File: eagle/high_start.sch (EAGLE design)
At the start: 34 parts, among them IC1 7805L, Q1 16Mhz, Q2 IRF510, Q3 IRF510, Q4 IRF510, U2 ATMEGA328P_PDIP

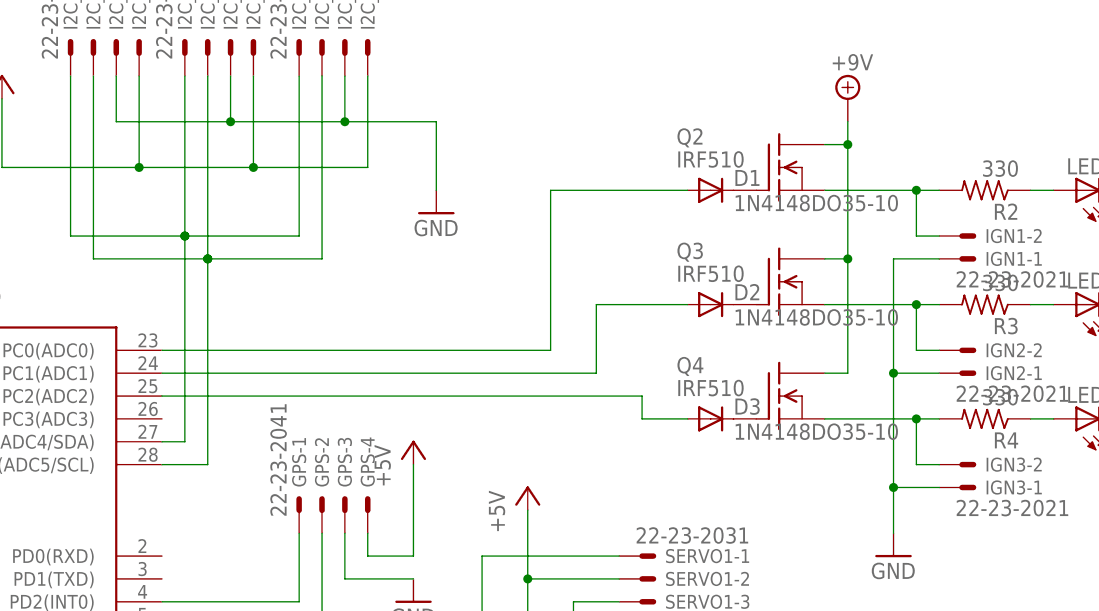
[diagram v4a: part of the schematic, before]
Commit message: board tweaks and three servos into code
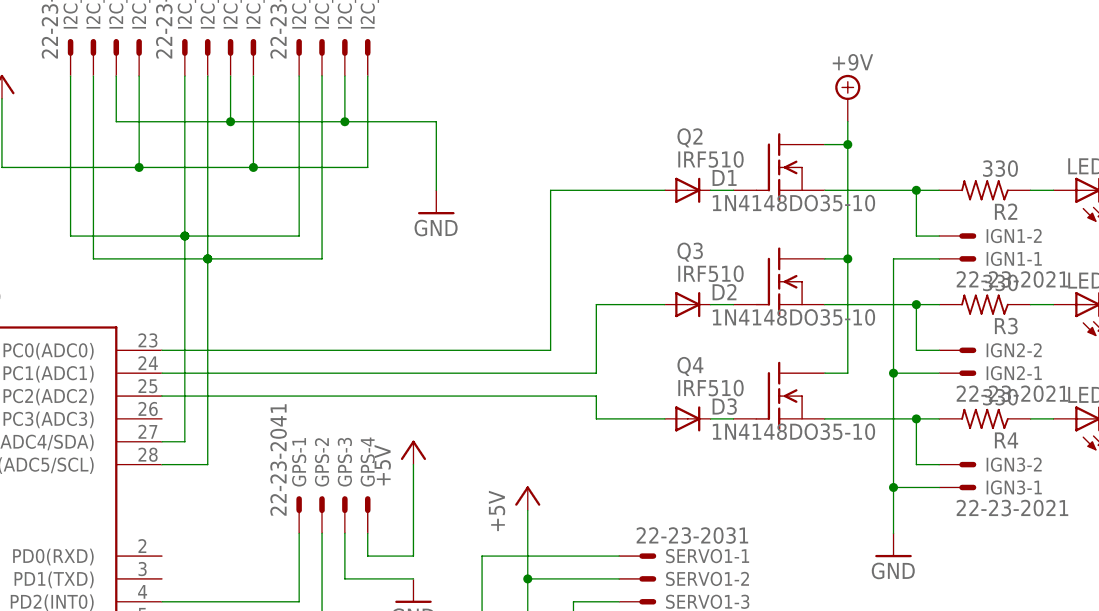
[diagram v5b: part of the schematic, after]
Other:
- moved on the sheet: D1, D2, D3
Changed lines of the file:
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@@
 <instance part="Q3" gate="G$1" x="109.22" y="81.28"/>
 <instance part="SUPPLY1" gate="G$1" x="116.84" y="101.6"/>
-<instance part="D1" gate="G$1" x="101.6" y="91.44"/>
-<instance part="D2" gate="G$1" x="101.6" y="78.74"/>
+<instance part="D1" gate="G$1" x="99.06" y="91.44"/>
+<instance part="D2" gate="G$1" x="99.06" y="78.74"/>
 <instance part="Q4" gate="G$1" x="109.22" y="68.58"/>
-<instance part="D3" gate="G$1" x="101.6" y="66.04"/>
+<instance part="D3" gate="G$1" x="99.06" y="66.04"/>
 <instance part="SERVO1" gate="-1" x="93.98" y="50.8"/>
 <instance part="SERVO1" gate="-2" x="93.98" y="48.26"/>
@@
 <pinref part="Q3" gate="G$1" pin="G"/>
 <pinref part="D2" gate="G$1" pin="C"/>
+<wire x1="101.6" y1="78.74" x2="104.14" y2="78.74" width="0.1524" layer="91"/>
 </segment>
 </net>
@@
 <pinref part="Q2" gate="G$1" pin="G"/>
 <pinref part="D1" gate="G$1" pin="C"/>
+<wire x1="101.6" y1="91.44" x2="104.14" y2="91.44" width="0.1524" layer="91"/>
 </segment>
 </net>
@@
 <pinref part="Q4" gate="G$1" pin="G"/>
 <pinref part="D3" gate="G$1" pin="C"/>
+<wire x1="101.6" y1="66.04" x2="104.14" y2="66.04" width="0.1524" layer="91"/>
 </segment>
 </net>
@@
 <wire x1="83.82" y1="73.66" x2="83.82" y2="91.44" width="0.1524" layer="91"/>
 <pinref part="D1" gate="G$1" pin="A"/>
-<wire x1="83.82" y1="91.44" x2="99.06" y2="91.44" width="0.1524" layer="91"/>
+<wire x1="83.82" y1="91.44" x2="96.52" y2="91.44" width="0.1524" layer="91"/>
 </segment>
 </net>
@@
 <wire x1="88.9" y1="71.12" x2="88.9" y2="78.74" width="0.1524" layer="91"/>
 <pinref part="D2" gate="G$1" pin="A"/>
-<wire x1="88.9" y1="78.74" x2="99.06" y2="78.74" width="0.1524" layer="91"/>
+<wire x1="88.9" y1="78.74" x2="96.52" y2="78.74" width="0.1524" layer="91"/>
 </segment>
 </net>
@@
 <segment>
 <pinref part="U2" gate="G$1" pin="PC2(ADC2)"/>
-<wire x1="40.64" y1="68.58" x2="93.98" y2="68.58" width="0.1524" layer="91"/>
-<wire x1="93.98" y1="68.58" x2="93.98" y2="66.04" width="0.1524" layer="91"/>
+<wire x1="40.64" y1="68.58" x2="88.9" y2="68.58" width="0.1524" layer="91"/>
+<wire x1="88.9" y1="68.58" x2="88.9" y2="66.04" width="0.1524" layer="91"/>
 <pinref part="D3" gate="G$1" pin="A"/>
-<wire x1="93.98" y1="66.04" x2="99.06" y2="66.04" width="0.1524" layer="91"/>
-</segment>
-</net>
+<wire x1="88.9" y1="66.04" x2="96.52" y2="66.04" width="0.1524" layer="91"/>
+</segment>
+</net>

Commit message: added airframe cam files to the repo
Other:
- moved on the sheet: IGN1-1, IGN1-2, IGN2-1, IGN2-2, IGN3-1, IGN3-2
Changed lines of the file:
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@@
 <part name="LED2" library="led" deviceset="LED" device="5MM"/>
 <part name="LED3" library="led" deviceset="LED" device="5MM"/>
-<part name="GND5" library="supply1" deviceset="GND" device=""/>
 <part name="GND6" library="supply1" deviceset="GND" device=""/>
 <part name="GPS" library="con-molex" deviceset="22-23-2041" device=""/>
@@
 <instance part="R3" gate="G$1" x="132.08" y="78.74" rot="R180"/>
 <instance part="R4" gate="G$1" x="132.08" y="66.04" rot="R180"/>
-<instance part="IGN1" gate="-1" x="129.54" y="83.82" rot="MR180"/>
-<instance part="IGN1" gate="-2" x="129.54" y="86.36" rot="MR180"/>
-<instance part="IGN2" gate="-1" x="129.54" y="71.12" rot="MR180"/>
-<instance part="IGN2" gate="-2" x="129.54" y="73.66" rot="MR180"/>
-<instance part="IGN3" gate="-1" x="129.54" y="58.42" rot="MR180"/>
-<instance part="IGN3" gate="-2" x="129.54" y="60.96" rot="MR180"/>
+<instance part="IGN1" gate="-1" x="144.78" y="86.36" rot="MR0"/>
+<instance part="IGN1" gate="-2" x="124.46" y="86.36" rot="MR180"/>
+<instance part="IGN2" gate="-1" x="144.78" y="73.66" rot="MR0"/>
+<instance part="IGN2" gate="-2" x="124.46" y="73.66" rot="MR180"/>
+<instance part="IGN3" gate="-1" x="144.78" y="60.96" rot="MR0"/>
+<instance part="IGN3" gate="-2" x="124.46" y="60.96" rot="MR180"/>
 <instance part="LED1" gate="G$1" x="142.24" y="91.44" rot="R90"/>
 <instance part="LED2" gate="G$1" x="142.24" y="78.74" rot="R90"/>
 <instance part="LED3" gate="G$1" x="142.24" y="66.04" rot="R90"/>
-<instance part="GND5" gate="1" x="121.92" y="50.8"/>
 <instance part="GND6" gate="1" x="149.86" y="50.8"/>
 <instance part="GPS" gate="-1" x="55.88" y="55.88" rot="R90"/>
@@
 </segment>
 <segment>
-<pinref part="IGN1" gate="-1" pin="S"/>
-<pinref part="GND5" gate="1" pin="GND"/>
-<wire x1="127" y1="83.82" x2="121.92" y2="83.82" width="0.1524" layer="91"/>
-<wire x1="121.92" y1="83.82" x2="121.92" y2="71.12" width="0.1524" layer="91"/>
-<pinref part="IGN3" gate="-1" pin="S"/>
-<wire x1="121.92" y1="71.12" x2="121.92" y2="58.42" width="0.1524" layer="91"/>
-<wire x1="121.92" y1="58.42" x2="121.92" y2="53.34" width="0.1524" layer="91"/>
-<wire x1="127" y1="58.42" x2="121.92" y2="58.42" width="0.1524" layer="91"/>
-<junction x="121.92" y="58.42"/>
-<pinref part="IGN2" gate="-1" pin="S"/>
-<wire x1="127" y1="71.12" x2="121.92" y2="71.12" width="0.1524" layer="91"/>
-<junction x="121.92" y="71.12"/>
-</segment>
-<segment>
 <pinref part="LED1" gate="G$1" pin="C"/>
 <pinref part="GND6" gate="1" pin="GND"/>
 <wire x1="147.32" y1="91.44" x2="149.86" y2="91.44" width="0.1524" layer="91"/>
-<wire x1="149.86" y1="91.44" x2="149.86" y2="78.74" width="0.1524" layer="91"/>
+<wire x1="149.86" y1="91.44" x2="149.86" y2="86.36" width="0.1524" layer="91"/>
 <pinref part="LED3" gate="G$1" pin="C"/>
-<wire x1="149.86" y1="78.74" x2="149.86" y2="66.04" width="0.1524" layer="91"/>
-<wire x1="149.86" y1="66.04" x2="149.86" y2="53.34" width="0.1524" layer="91"/>
+<wire x1="149.86" y1="86.36" x2="149.86" y2="78.74" width="0.1524" layer="91"/>
+<wire x1="149.86" y1="78.74" x2="149.86" y2="73.66" width="0.1524" layer="91"/>
+<wire x1="149.86" y1="73.66" x2="149.86" y2="66.04" width="0.1524" layer="91"/>
+<wire x1="149.86" y1="66.04" x2="149.86" y2="60.96" width="0.1524" layer="91"/>
+<wire x1="149.86" y1="60.96" x2="149.86" y2="53.34" width="0.1524" layer="91"/>
 <wire x1="147.32" y1="66.04" x2="149.86" y2="66.04" width="0.1524" layer="91"/>
 <junction x="149.86" y="66.04"/>
@@
 <wire x1="147.32" y1="78.74" x2="149.86" y2="78.74" width="0.1524" layer="91"/>
 <junction x="149.86" y="78.74"/>
+<pinref part="IGN1" gate="-1" pin="S"/>
+<wire x1="147.32" y1="86.36" x2="149.86" y2="86.36" width="0.1524" layer="91"/>
+<junction x="149.86" y="86.36"/>
+<pinref part="IGN2" gate="-1" pin="S"/>
+<wire x1="147.32" y1="73.66" x2="149.86" y2="73.66" width="0.1524" layer="91"/>
+<junction x="149.86" y="73.66"/>
+<pinref part="IGN3" gate="-1" pin="S"/>
+<wire x1="147.32" y1="60.96" x2="149.86" y2="60.96" width="0.1524" layer="91"/>
+<junction x="149.86" y="60.96"/>
 </segment>
 <segment>
@@
 <pinref part="Q2" gate="G$1" pin="S"/>
 <pinref part="R2" gate="G$1" pin="2"/>
-<wire x1="114.3" y1="91.44" x2="124.46" y2="91.44" width="0.1524" layer="91"/>
+<wire x1="114.3" y1="91.44" x2="121.92" y2="91.44" width="0.1524" layer="91"/>
 <pinref part="IGN1" gate="-2" pin="S"/>
-<wire x1="124.46" y1="91.44" x2="127" y2="91.44" width="0.1524" layer="91"/>
-<wire x1="127" y1="86.36" x2="124.46" y2="86.36" width="0.1524" layer="91"/>
-<wire x1="124.46" y1="86.36" x2="124.46" y2="91.44" width="0.1524" layer="91"/>
-<junction x="124.46" y="91.44"/>
+<wire x1="121.92" y1="91.44" x2="127" y2="91.44" width="0.1524" layer="91"/>
+<wire x1="121.92" y1="86.36" x2="121.92" y2="91.44" width="0.1524" layer="91"/>
+<junction x="121.92" y="91.44"/>
 </segment>
 </net>
@@
 <pinref part="Q3" gate="G$1" pin="S"/>
 <pinref part="R3" gate="G$1" pin="2"/>
-<wire x1="114.3" y1="78.74" x2="124.46" y2="78.74" width="0.1524" layer="91"/>
+<wire x1="114.3" y1="78.74" x2="121.92" y2="78.74" width="0.1524" layer="91"/>
 <pinref part="IGN2" gate="-2" pin="S"/>
-<wire x1="124.46" y1="78.74" x2="127" y2="78.74" width="0.1524" layer="91"/>
-<wire x1="127" y1="73.66" x2="124.46" y2="73.66" width="0.1524" layer="91"/>
-<wire x1="124.46" y1="73.66" x2="124.46" y2="78.74" width="0.1524" layer="91"/>
-<junction x="124.46" y="78.74"/>
+<wire x1="121.92" y1="78.74" x2="127" y2="78.74" width="0.1524" layer="91"/>
+<wire x1="121.92" y1="73.66" x2="121.92" y2="78.74" width="0.1524" layer="91"/>
+<junction x="121.92" y="78.74"/>
 </segment>
 </net>
@@
 <pinref part="Q4" gate="G$1" pin="S"/>
 <pinref part="R4" gate="G$1" pin="2"/>
-<wire x1="114.3" y1="66.04" x2="124.46" y2="66.04" width="0.1524" layer="91"/>
+<wire x1="114.3" y1="66.04" x2="121.92" y2="66.04" width="0.1524" layer="91"/>
 <pinref part="IGN3" gate="-2" pin="S"/>
-<wire x1="124.46" y1="66.04" x2="127" y2="66.04" width="0.1524" layer="91"/>
-<wire x1="127" y1="60.96" x2="124.46" y2="60.96" width="0.1524" layer="91"/>
-<wire x1="124.46" y1="60.96" x2="124.46" y2="66.04" width="0.1524" layer="91"/>
-<junction x="124.46" y="66.04"/>
-</segment>
-</net>
+<wire x1="121.92" y1="66.04" x2="127" y2="66.04" width="0.1524" layer="91"/>
+<wire x1="121.92" y1="60.96" x2="121.92" y2="66.04" width="0.1524" layer="91"/>
+<junction x="121.92" y="66.04"/>
+</segment>
+</net>

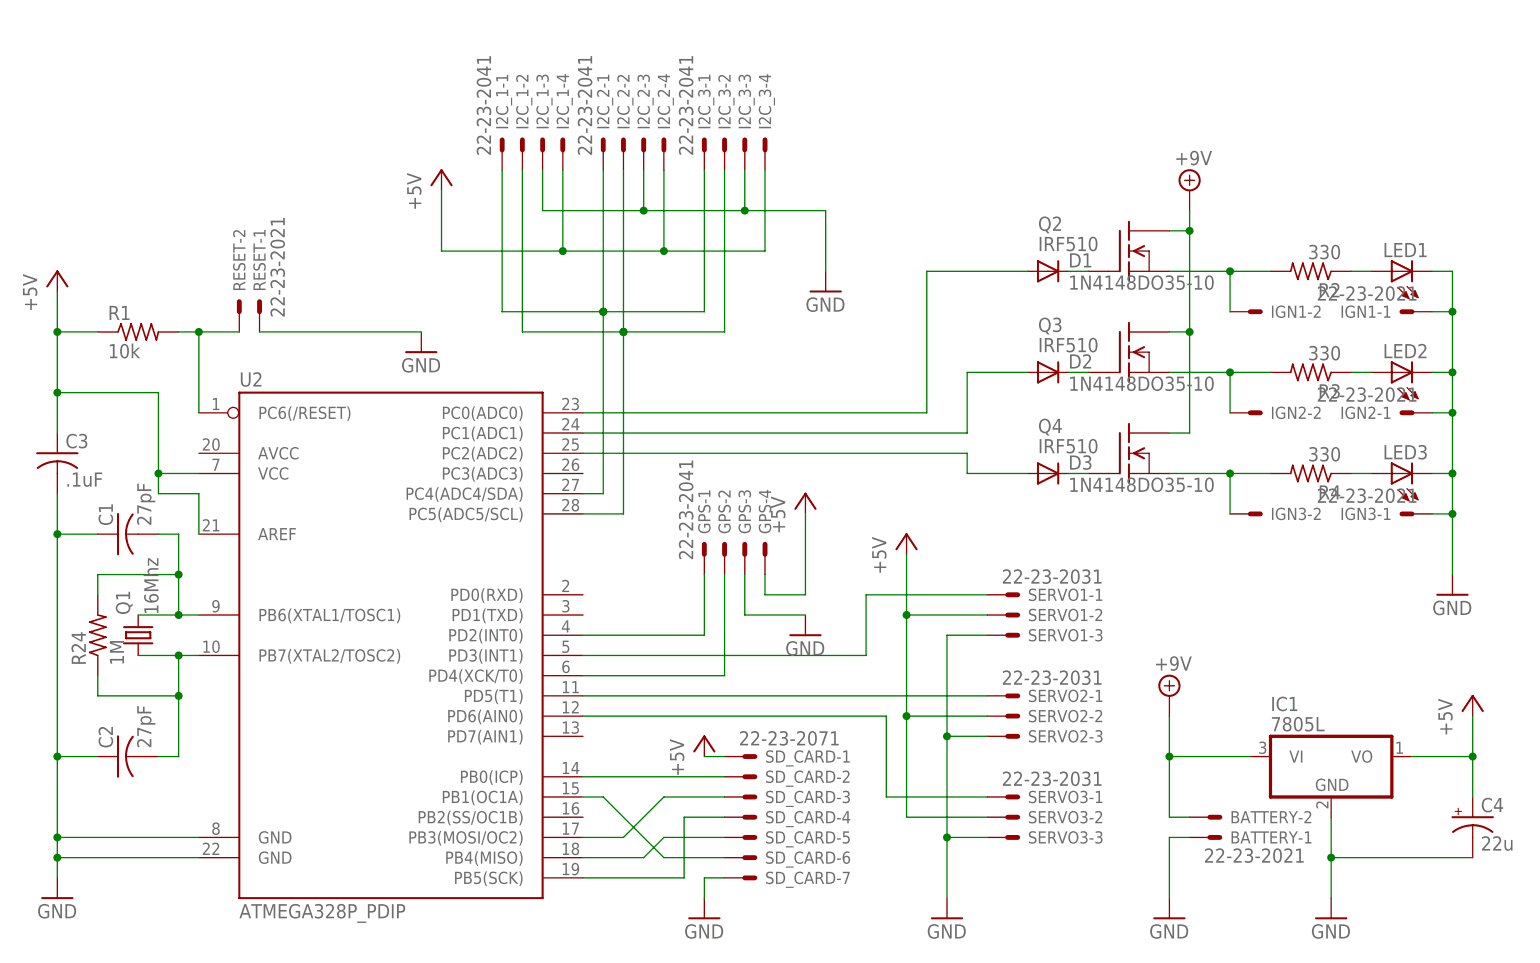
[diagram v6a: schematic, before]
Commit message: pulldown resistors onto schemo
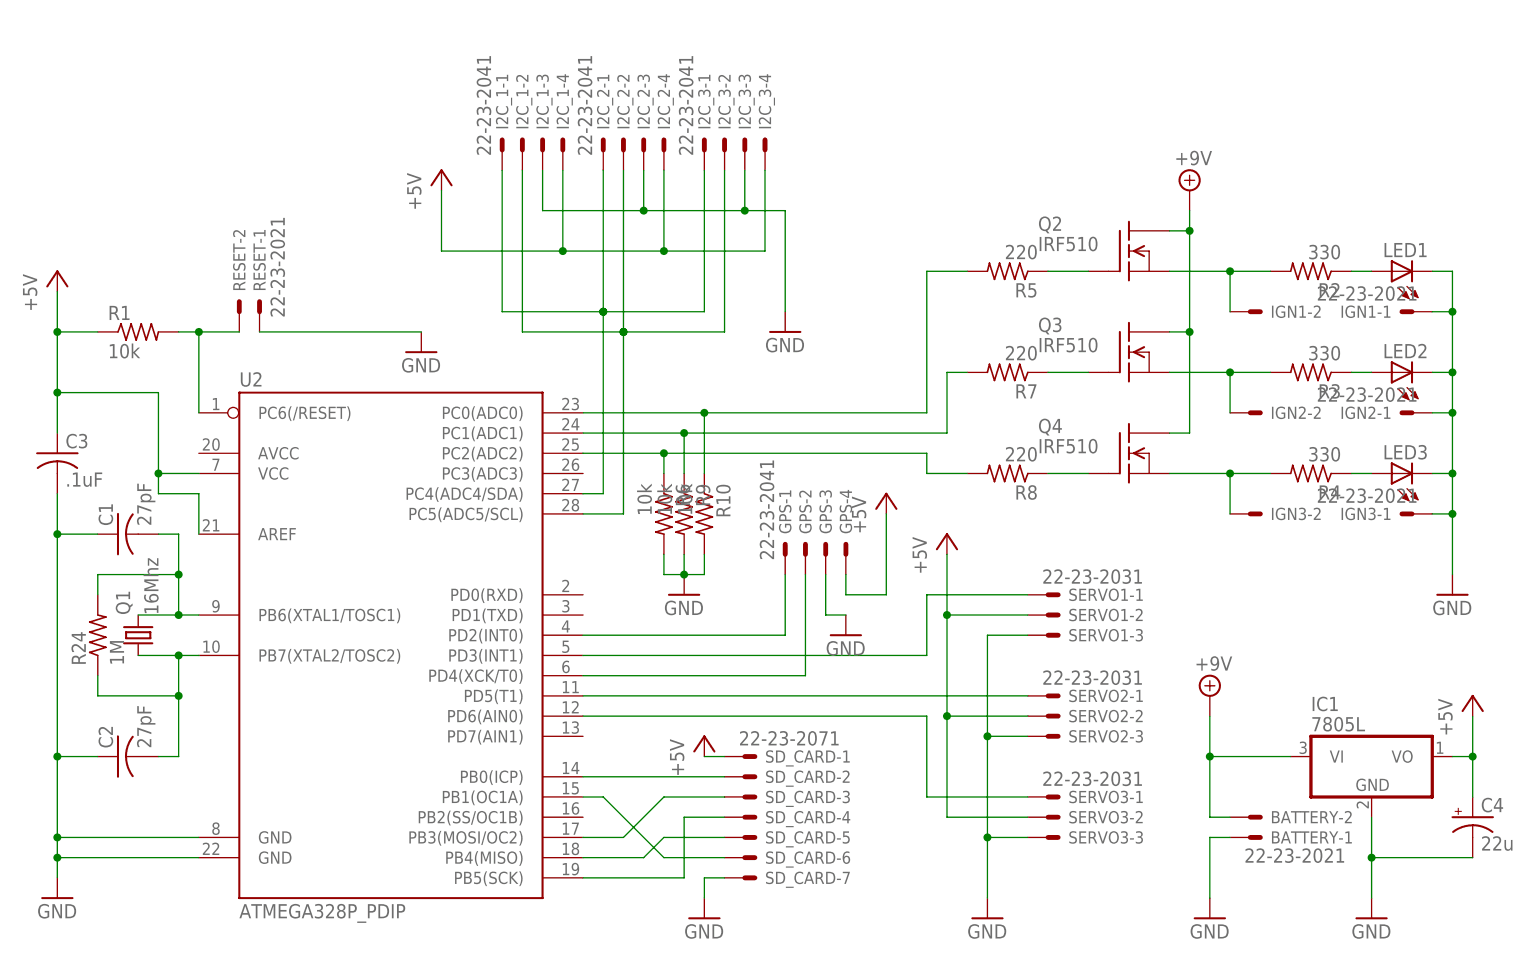
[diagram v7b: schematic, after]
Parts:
- removed D1, D2, D3: 1N4148DO35-10, diode:1N4148DO35-10
- added R10, R6, R9: 10k, rcl:R-US_0207/7
- added R5, R7, R8: 220, rcl:R-US_0207/7
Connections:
- net GND: now also R10.2, R6.2, R9.2
- net N$12: now also Q2.G, R5.1; no longer D2.C, Q3.G
- net N$13: now also Q3.G, R7.1; no longer D1.C, Q2.G
- net N$14: now also R8.1; no longer D3.C
- net N$18: now also R10.1, R5.2; no longer D1.A
- net N$19: now also R7.2, R9.1; no longer D2.A
- net N$20: now also R6.1, R8.2; no longer D3.A
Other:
- moved on the sheet: BATTERY-1, BATTERY-2, GPS-1, GPS-2, GPS-3, GPS-4, IC1, SERVO1-1, SERVO1-2, SERVO1-3, SERVO2-1, SERVO2-2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
